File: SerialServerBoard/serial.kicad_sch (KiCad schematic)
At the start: 19 parts, among them J6 ASSMANN A-DF 09 A/KG-T2S, U2 MAX3237EIPWR

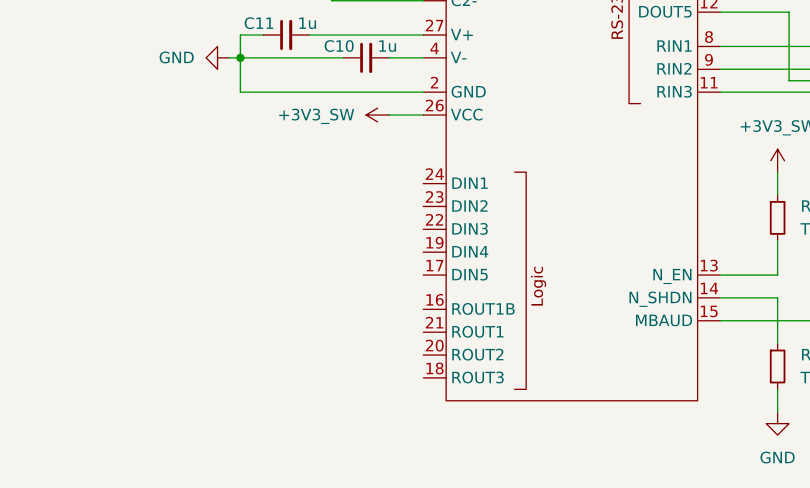
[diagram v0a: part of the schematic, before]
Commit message: Add ATECC
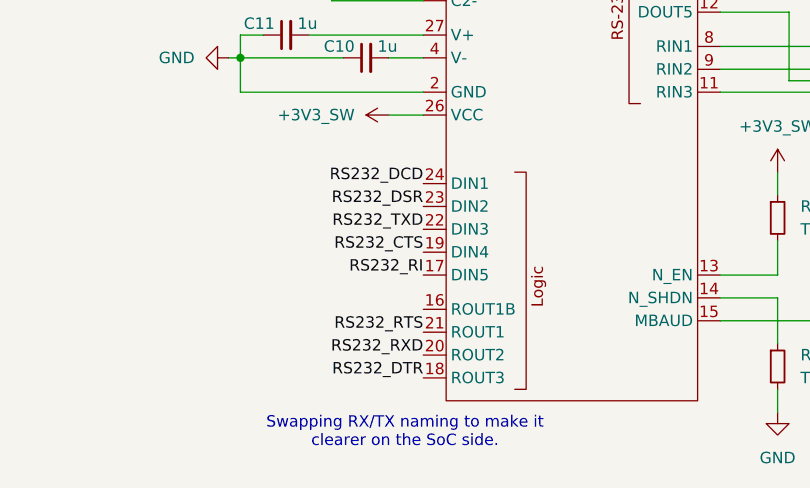
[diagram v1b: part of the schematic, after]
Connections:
- net RS232_RI: now reaches U2.17 (DIN5)
- net RS232_DTR: now reaches U2.18 (ROUT3)
- net RS232_CTS: now reaches U2.19 (DIN4)
- net RS232_RXD: now reaches U2.20 (ROUT2)
- net RS232_RTS: now reaches U2.21 (ROUT1)
- net RS232_TXD: now reaches U2.22 (DIN3)
- net RS232_DSR: now reaches U2.23 (DIN2)
- net RS232_DCD: now reaches U2.24 (DIN1)
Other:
- note added: "Swapping RX/TX naming to make it clearer on the SoC side."
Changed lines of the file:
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@@
+		)
+	)
+	(text "Swapping RX/TX naming to make it\nclearer on the SoC side."
+		(exclude_from_sim no)
+		(at 154.178 86.106 0)
+		(effects
+			(font
+				(size 1.27 1.27)
+			)
 		)
 	)
@@
 			)
 			(justify left bottom)
+		)
+	)
+	(label "RS232_DTR"
+		(at 156.21 80.01 180)
+		(fields_autoplaced yes)
+		(effects
+			(font
+				(size 1.27 1.27)
+			)
+			(justify right bottom)
+		)
+	)
+	(label "RS232_RXD"
+		(at 156.21 77.47 180)
+		(fields_autoplaced yes)
+		(effects
+			(font
+				(size 1.27 1.27)
+			)
+			(justify right bottom)
+		)
+	)
+	(label "RS232_DSR"
+		(at 156.21 60.96 180)
+		(fields_autoplaced yes)
+		(effects
+			(font
+				(size 1.27 1.27)
+			)
+			(justify right bottom)
+		)
+	)
+	(label "RS232_RI"
+		(at 156.21 68.58 180)
+		(fields_autoplaced yes)
+		(effects
+			(font
+				(size 1.27 1.27)
+			)
+			(justify right bottom)
 		)
 	)
@@
 		)
 	)
+	(label "RS232_CTS"
+		(at 156.21 66.04 180)
+		(fields_autoplaced yes)
+		(effects
+			(font
+				(size 1.27 1.27)
+			)
+			(justify right bottom)
+		)
+	)
 	(label "DE9_DTR"
 		(at 245.11 44.45 0)
@@
 			)
 			(justify left bottom)
+		)
+	)
+	(label "RS232_TXD"
+		(at 156.21 63.5 180)
+		(fields_autoplaced yes)
+		(effects
+			(font
+				(size 1.27 1.27)
+			)
+			(justify right bottom)
 		)
 	)
@@
 		)
 	)
+	(label "RS232_DCD"
+		(at 156.21 58.42 180)
+		(fields_autoplaced yes)
+		(effects
+			(font
+				(size 1.27 1.27)
+			)
+			(justify right bottom)
+		)
+	)
 	(label "DE9_TXD"
 		(at 245.11 39.37 0)
@@
 		)
 	)
+	(label "RS232_RTS"
+		(at 156.21 74.93 180)
+		(fields_autoplaced yes)
+		(effects
+			(font
+				(size 1.27 1.27)
+			)
+			(justify right bottom)
+		)
+	)

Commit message: Add micro-SD card slot
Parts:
- added J11: DE9, Connector_PinHeader_1.27mm:PinHeader_1x09_P1.27mm_Vertical, symbol Connector:Conn_01x09_Socket
- added J12: Control, Connector_PinHeader_1.27mm:PinHeader_1x10_P1.27mm_Vertical, symbol Connector:Conn_01x10_Socket
- added J13: Comms, Connector_PinHeader_1.27mm:PinHeader_1x06_P1.27mm_Vertical, symbol Connector:Conn_01x06_Socket
- added R35: 0, Resistor_SMD:R_0402_1005Metric, symbol Device:R_Small
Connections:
- net +3V3_SW: now also J12.10 (Pin_10)
- net DE9_CTS: now also J11.8 (Pin_8)
- net DE9_DCD: now also J11.1 (Pin_1)
- net DE9_DSR: now also J11.6 (Pin_6)
- net DE9_DTR: now also J11.4 (Pin_4)
- net DE9_RI: now also J11.9 (Pin_9)
- net DE9_RTS: now also J11.7 (Pin_7)
- net DE9_RXD: now also J11.2 (Pin_2)
- net DE9_TXD: now also J11.3 (Pin_3)
- net GND: now also J11.5 (Pin_5), J12.5 (Pin_5), R35.1; no longer J6.5
- net RS232_CTS: now also J12.8 (Pin_8)
- net RS232_DCD: now also J12.1 (Pin_1)
- net RS232_DSR: now also J12.6 (Pin_6)
- net RS232_DTR: now also J12.4 (Pin_4)
- net RS232_RI: now also J12.9 (Pin_9)
- net RS232_RTS: now also J12.7 (Pin_7)
- net RS232_RXD: now also J12.3 (Pin_3)
- net RS232_TXD: now also J12.2 (Pin_2)
- new net: J6.5, R35.2
- new net I2C_SCL: J13.1 (Pin_1)
- new net I2C_SDA: J13.2 (Pin_2)
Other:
- note added: "Connectors for supporting different modules for different signaling, connectors, or additional ports."
